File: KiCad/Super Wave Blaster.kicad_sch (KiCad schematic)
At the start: 42 parts, among them U1 TLV73333PDBV, U2 CD74HCT14PWR, U3 SN74HC595PWR, U4 SN74LVC8T245PWR, U5 PCM5102A

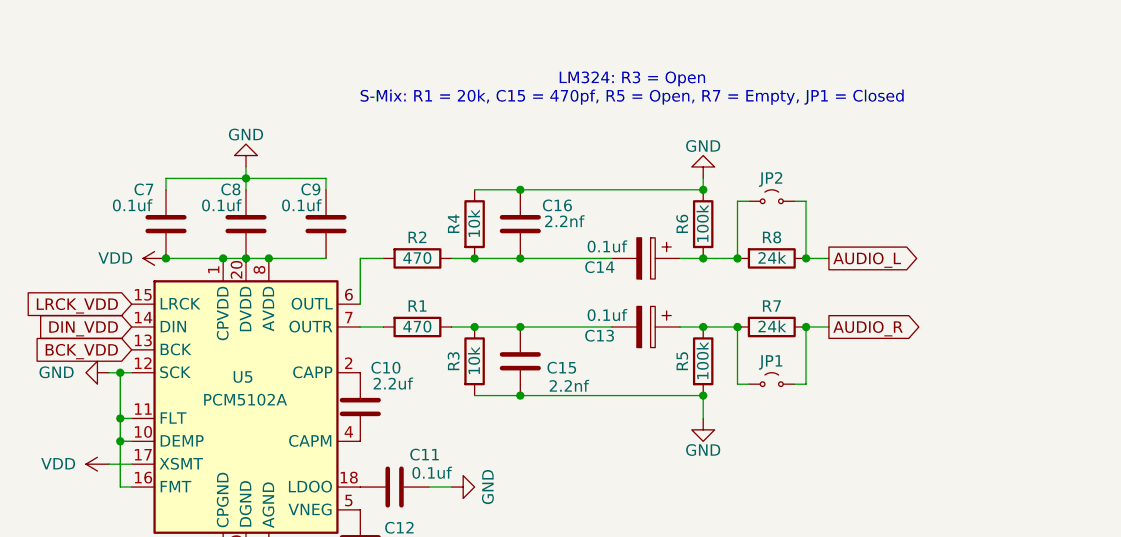
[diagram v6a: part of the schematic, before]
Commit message: Update README and schematic documentation. Save with newer version of Kicad
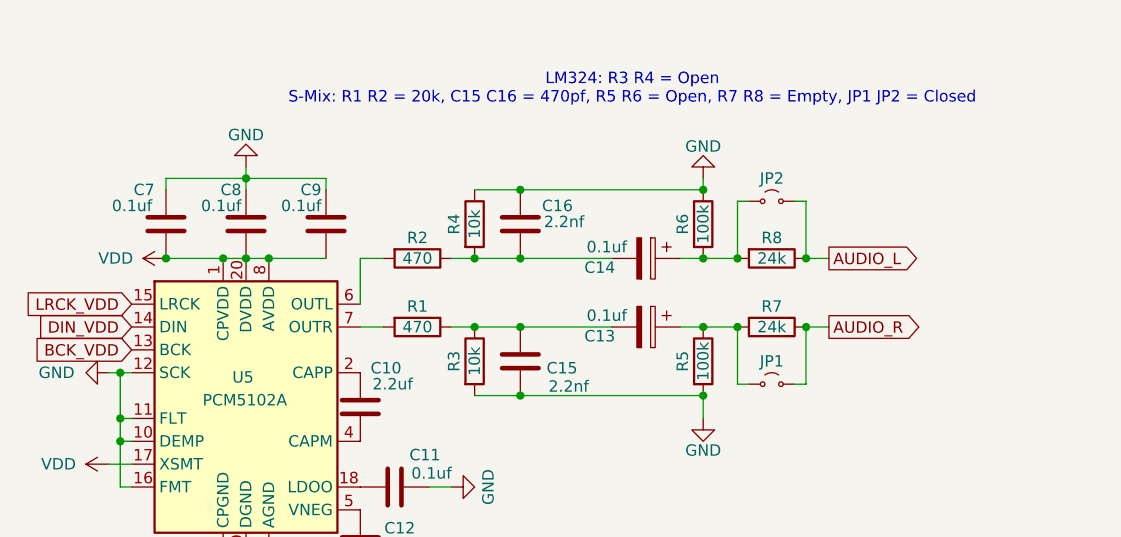
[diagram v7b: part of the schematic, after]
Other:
- note added: "LM324: R3 R4 = Open S-Mix: R1 R2 = 20k, C15 C16 = 470pf, R5 R6 = Open, R7 R8 = Empty, JP1 JP2 = Closed"
- note removed: "LM324: R3 = Open S-Mix: R1 = 20k, C15 = 470pf, R5 = Open, R7 = Empty, JP1 = Closed"
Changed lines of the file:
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@@
 (kicad_sch
-	(version 20231120)
+	(version 20250114)
 	(generator "eeschema")
-	(generator_version "8.0")
+	(generator_version "9.0")
 	(paper "A4")
+	(text "LM324: R3 R4 = Open\nS-Mix: R1 R2 = 20k, C15 C16 = 470pf, R5 R6 = Open, R7 R8 = Empty, JP1 JP2 = Closed"
+		(exclude_from_sim no)
+		(at 238.506 25.654 0)
+		(effects
+			(font
+				(size 1.27 1.27)
+			)
+		)
+	)
 	(junction
 		(at 246.38 52.07)
@@
 		)
 	)
-	(text "LM324: R3 = Open\nS-Mix: R1 = 20k, C15 = 470pf, R5 = Open, R7 = Empty, JP1 = Closed"
-		(exclude_from_sim no)
-		(at 238.506 25.654 0)
-		(effects
-			(font
-				(size 1.27 1.27)
-			)
-		)
-	)
 	(global_label "BCK_VDD"
 		(shape input)
@@
 		)
 	)
+	(embedded_fonts no)
 )

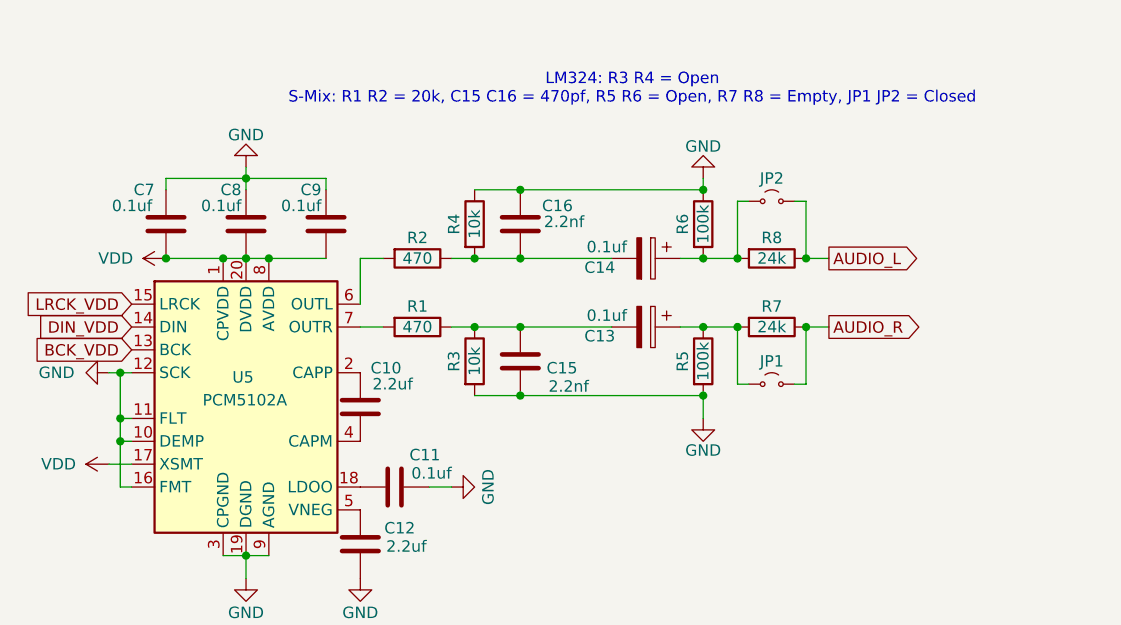
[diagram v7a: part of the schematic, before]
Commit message: v1.7 - Fix issue with high pass pole, add MDF measurements, update layout for changes with X7R coupling caps
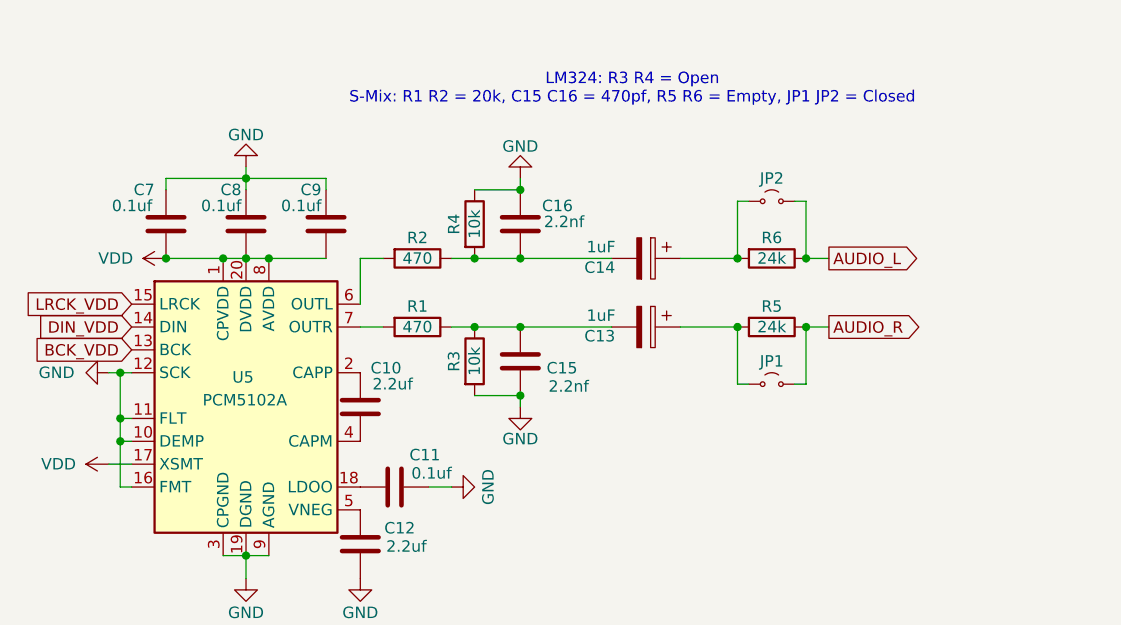
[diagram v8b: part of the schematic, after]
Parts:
- removed R5, R6: 100k, Resistor_SMD:R_0805_2012Metric_Pad1.20x1.40mm_HandSolder, symbol Device:R
- C13, C14: value 0.1uf -> 1uF; footprint Capacitor_SMD:C_1206_3216Metric_Pad1.33x1.80mm_HandSolder -> Capacitor_SMD:C_0805_2012Metric_Pad1.18x1.45mm_HandSolder
- renumbered R7 to R5, R8 to R6
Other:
- note added: "LM324: R3 R4 = Open S-Mix: R1 R2 = 20k, C15 C16 = 470pf, R5 R6 = Empty, JP1 JP2 = Closed"
- note removed: "LM324: R3 R4 = Open S-Mix: R1 R2 = 20k, C15 C16 = 470pf, R5 R6 = Open, R7 R8 = Empty, JP1 JP2 = Closed"
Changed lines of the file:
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@@
 	(generator_version "9.0")
 	(paper "A4")
-	(text "LM324: R3 R4 = Open\nS-Mix: R1 R2 = 20k, C15 C16 = 470pf, R5 R6 = Open, R7 R8 = Empty, JP1 JP2 = Closed"
+	(text "LM324: R3 R4 = Open\nS-Mix: R1 R2 = 20k, C15 C16 = 470pf, R5 R6 = Empty, JP1 JP2 = Closed"
 		(exclude_from_sim no)
 		(at 238.506 25.654 0)
@@
 	)
 	(junction
-		(at 246.38 52.07)
-		(diameter 0)
-		(color 0 0 0 0)
-	)
-	(junction
 		(at 49.53 34.29)
 		(diameter 0)
@@
 	)
 	(junction
-		(at 246.38 59.69)
-		(diameter 0)
-		(color 0 0 0 0)
-	)
-	(junction
 		(at 257.81 52.07)
 		(diameter 0)
@@
 	)
 	(junction
-		(at 246.38 36.83)
-		(diameter 0)
-		(color 0 0 0 0)
-	)
-	(junction
 		(at 250.19 52.07)
 		(diameter 0)
@@
 	)
 	(junction
-		(at 246.38 44.45)
-		(diameter 0)
-		(color 0 0 0 0)
-	)
-	(junction
 		(at 181.61 57.15)
 		(diameter 0)
@@
 	(wire
 		(pts
-			(xy 243.84 44.45) (xy 246.38 44.45)
-		)
-		(stroke
-			(width 0)
-			(type default)
-		)
-	)
-	(wire
-		(pts
 			(xy 143.51 44.45) (xy 144.78 44.45)
 		)
@@
 	(wire
 		(pts
-			(xy 246.38 35.56) (xy 246.38 36.83)
+			(xy 226.06 35.56) (xy 226.06 36.83)
 		)
 		(stroke
@@
 	(wire
 		(pts
-			(xy 243.84 52.07) (xy 246.38 52.07)
+			(xy 243.84 52.07) (xy 250.19 52.07)
 		)
 		(stroke
@@
 	(wire
 		(pts
-			(xy 246.38 44.45) (xy 250.19 44.45)
+			(xy 243.84 44.45) (xy 250.19 44.45)
 		)
 		(stroke
@@
 	(wire
 		(pts
-			(xy 226.06 36.83) (xy 246.38 36.83)
-		)
-		(stroke
-			(width 0)
-			(type default)
-		)
-	)
-	(wire
-		(pts
 			(xy 57.15 111.76) (xy 57.15 109.22)
 		)
@@
 	(wire
 		(pts
-			(xy 226.06 59.69) (xy 246.38 59.69)
-		)
-		(stroke
-			(width 0)
-			(type default)
-		)
-	)
-	(wire
-		(pts
 			(xy 256.54 58.42) (xy 257.81 58.42)
 		)
@@
 	(wire
 		(pts
-			(xy 246.38 59.69) (xy 246.38 62.23)
+			(xy 226.06 59.69) (xy 226.06 60.96)
 		)
 		(stroke
@@
 	(wire
 		(pts
-			(xy 246.38 52.07) (xy 250.19 52.07)
-		)
-		(stroke
-			(width 0)
-			(type default)
-		)
-	)
-	(wire
-		(pts
 			(xy 144.78 44.45) (xy 147.32 44.45)
 		)
@@
 			)
 		)
-		(property "Value" "0.1uf"
+		(property "Value" "1uF"
 			(at 233.426 50.8 90)
 			(effects
@@
 			)
 		)
-		(property "Footprint" "Capacitor_SMD:C_1206_3216Metric_Pad1.33x1.80mm_HandSolder"
+		(property "Footprint" "Capacitor_SMD:C_0805_2012Metric_Pad1.18x1.45mm_HandSolder"
 			(at 236.22 53.0352 0)
 			(effects
@@
 		(on_board yes)
 		(dnp no)
-		(property "Reference" "R7"
+		(property "Reference" "R5"
 			(at 254 49.784 90)
 			(effects
@@
 			(project "Super Wave Blaster"
 				(path "/a781822e-a133-40a7-b35d-245c79924aaa"
-					(reference "R7")
+					(reference "R5")
 					(unit 1)
 				)
@@
 	)
 	(symbol
-		(lib_id "Device:R")
-		(at 246.38 40.64 0)
-		(unit 1)
-		(exclude_from_sim no)
-		(in_bom yes)
-		(on_board yes)
-		(dnp no)
-		(property "Reference" "R6"
-			(at 244.094 40.64 90)
-			(effects
-				(font
-					(size 1.27 1.27)
-				)
-			)
-		)
-		(property "Value" "100k"
-			(at 246.38 40.64 90)
-			(effects
-				(font
-					(size 1.27 1.27)
-				)
-			)
-		)
-		(property "Footprint" "Resistor_SMD:R_0805_2012Metric_Pad1.20x1.40mm_HandSolder"
-			(at 244.602 40.64 90)
-			(effects
-				(font
-					(size 1.27 1.27)
-				)
-				(hide yes)
-			)
-		)
-		(property "Datasheet" "~"
-			(at 246.38 40.64 0)
-			(effects
-				(font
-					(size 1.27 1.27)
-				)
-				(hide yes)
-			)
-		)
-		(property "Description" "Resistor"
-			(at 246.38 40.64 0)
-			(effects
-				(font
-					(size 1.27 1.27)
-				)
-				(hide yes)
-			)
-		)
-		(pin "1"
-		)
-		(pin "2"
-		)
-		(instances
-			(project ""
-				(path "/a781822e-a133-40a7-b35d-245c79924aaa"
-					(reference "R6")
-					(unit 1)
-				)
-			)
-		)
-	)
-	(symbol
 		(lib_id "Device:C_Polarized")
 		(at 240.03 44.45 270)
@@
 			)
 		)
-		(property "Value" "0.1uf"
+		(property "Value" "1uF"
 			(at 233.426 43.18 90)
 			(effects
@@
 			)
 		)
-		(property "Footprint" "Capacitor_SMD:C_1206_3216Metric_Pad1.33x1.80mm_HandSolder"
+		(property "Footprint" "Capacitor_SMD:C_0805_2012Metric_Pad1.18x1.45mm_HandSolder"
 			(at 236.22 45.4152 0)
 			(effects
@@
 		(on_board yes)
 		(dnp no)
-		(property "Reference" "R8"
+		(property "Reference" "R6"
 			(at 254 42.164 90)
 			(effects
@@
 			(project "Super Wave Blaster"
 				(path "/a781822e-a133-40a7-b35d-245c79924aaa"
-					(reference "R8")
+					(reference "R6")
 					(unit 1)
 				)
@@
 	)
 	(symbol
-		(lib_id "Device:R")
-		(at 246.38 55.88 0)
-		(unit 1)
-		(exclude_from_sim no)
-		(in_bom yes)
-		(on_board yes)
-		(dnp no)
-		(property "Reference" "R5"
-			(at 244.094 55.88 90)
-			(effects
-				(font
-					(size 1.27 1.27)
-				)
-			)
-		)
-		(property "Value" "100k"
-			(at 246.38 55.88 90)
-			(effects
-				(font
-					(size 1.27 1.27)
-				)
-			)
-		)
-		(property "Footprint" "Resistor_SMD:R_0805_2012Metric_Pad1.20x1.40mm_HandSolder"
-			(at 244.602 55.88 90)
-			(effects
-				(font
-					(size 1.27 1.27)
-				)
-				(hide yes)
-			)
-		)
-		(property "Datasheet" "~"
-			(at 246.38 55.88 0)
-			(effects
-				(font
-					(size 1.27 1.27)
-				)
-				(hide yes)
-			)
-		)
-		(property "Description" "Resistor"
-			(at 246.38 55.88 0)
-			(effects
-				(font
-					(size 1.27 1.27)
-				)
-				(hide yes)
-			)
-		)
-		(pin "1"
-		)
-		(pin "2"
-		)
-		(instances
-			(project "Super Wave Blaster"
-				(path "/a781822e-a133-40a7-b35d-245c79924aaa"
-					(reference "R5")
-					(unit 1)
-				)
-			)
-		)
-	)
-	(symbol
 		(lib_id "power:GND")
 		(at 43.18 68.58 270)
@@
 	(symbol
 		(lib_id "power:GND")
-		(at 246.38 62.23 0)
+		(at 226.06 60.96 0)
 		(unit 1)
 		(exclude_from_sim no)
@@
 		(dnp no)
 		(property "Reference" "#PWR01"
-			(at 246.38 68.58 0)
+			(at 226.06 67.31 0)
 			(effects
 				(font
@@
 		)
 		(property "Value" "GND"
-			(at 246.38 65.786 0)
+			(at 226.06 64.516 0)
 			(effects
 				(font
@@
 		)
 		(property "Footprint" ""
-			(at 246.38 62.23 0)
+			(at 226.06 60.96 0)
 			(effects
 				(font
@@
 		)
 		(property "Datasheet" ""
-			(at 246.38 62.23 0)
+			(at 226.06 60.96 0)
 			(effects
 				(font
@@
 		)
 		(property "Description" ""
-			(at 246.38 62.23 0)
+			(at 226.06 60.96 0)
 			(effects
 				(font
@@
 	(symbol
 		(lib_id "power:GND")
-		(at 246.38 35.56 180)
+		(at 226.06 35.56 180)
 		(unit 1)
 		(exclude_from_sim no)
@@
 		(dnp no)
 		(property "Reference" "#PWR037"
-			(at 246.38 29.21 0)
+			(at 226.06 29.21 0)
 			(effects
 				(font
@@
 		)
 		(property "Value" "GND"
-			(at 246.38 32.004 0)
+			(at 226.06 32.004 0)
 			(effects
 				(font
@@
 		)
 		(property "Footprint" ""
-			(at 246.38 35.56 0)
+			(at 226.06 35.56 0)
 			(effects
 				(font
@@
 		)
 		(property "Datasheet" ""
-			(at 246.38 35.56 0)
+			(at 226.06 35.56 0)
 			(effects
 				(font
@@
 		)
 		(property "Description" ""
-			(at 246.38 35.56 0)
+			(at 226.06 35.56 0)
 			(effects
 				(font
